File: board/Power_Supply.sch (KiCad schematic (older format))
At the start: 6 parts, among them U3 TC1015-3.3VCT713

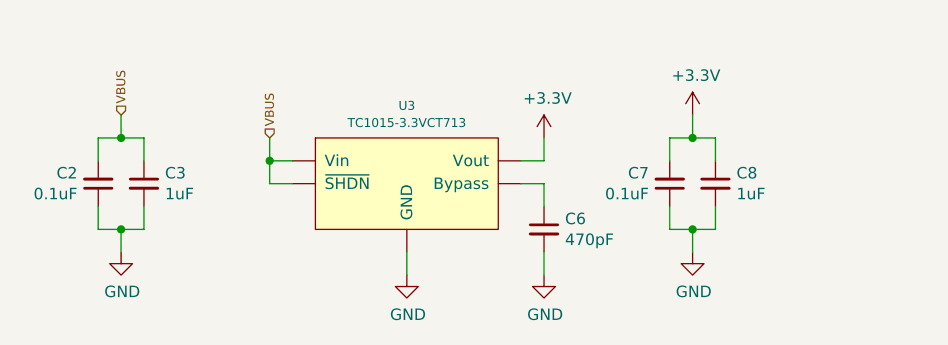
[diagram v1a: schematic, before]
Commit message: Added an LED to indicate the main board power status
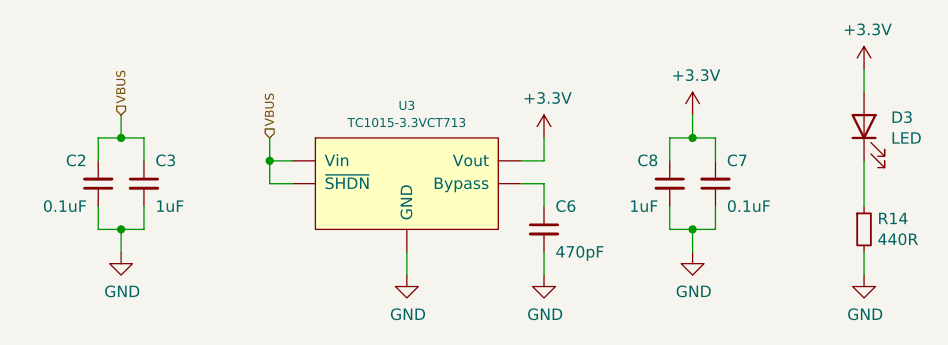
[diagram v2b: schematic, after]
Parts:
- added D3: LED, rhais_led:LED0603, symbol Device:LED
- added R14: 440R, rhais_rcl:R0603, symbol Device:R_Small
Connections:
- net +3V3: now also D3.2 (A)
- net GND: now also R14.2
- new net: D3.1 (K), R14.1
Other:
- moved on the sheet: C7, C8
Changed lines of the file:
@@
 U 1 1 5F6E72D6
 P 5600 4200
-F 0 "C6" H 5692 4246 50  0000 L CNN
-F 1 "470pF" H 5692 4155 50  0000 L CNN
+F 0 "C6" H 5650 4300 50  0000 L CNN
+F 1 "470pF" H 5650 4100 50  0000 L CNN
 F 2 "rhais_rcl:C0603" H 5600 4200 50  0001 C CNN
 F 3 "~" H 5600 4200 50  0001 C CNN
@@
 U 1 1 5F6E7C90
 P 3850 4000
-F 0 "C3" H 3942 4046 50  0000 L CNN
-F 1 "1uF" H 3942 3955 50  0000 L CNN
+F 0 "C3" H 3900 4100 50  0000 L CNN
+F 1 "1uF" H 3900 3900 50  0000 L CNN
 F 2 "rhais_rcl:C0603" H 3850 4000 50  0001 C CNN
 F 3 "~" H 3850 4000 50  0001 C CNN
@@
 U 1 1 5F6E812F
 P 3650 4000
-F 0 "C2" H 3559 3954 50  0000 R CNN
-F 1 "0.1uF" H 3559 4045 50  0000 R CNN
+F 0 "C2" H 3600 3900 50  0000 R CNN
+F 1 "0.1uF" H 3600 4100 50  0000 R CNN
 F 2 "rhais_rcl:C0603" H 3650 4000 50  0001 C CNN
 F 3 "~" H 3650 4000 50  0001 C CNN
@@
 L Device:C_Small C8
 U 1 1 5F6E94E9
+P 6150 4000
+F 0 "C8" H 6200 4100 50  0000 L CNN
+F 1 "1uF" H 6200 3900 50  0000 L CNN
+F 2 "rhais_rcl:C0603" H 6150 4000 50  0001 C CNN
+F 3 "~" H 6150 4000 50  0001 C CNN
+	1    6150 4000
+	-1   0    0    -1
+$EndComp
+$Comp
+L Device:C_Small C7
+U 1 1 5F6E94EF
 P 6350 4000
-F 0 "C8" H 6442 4046 50  0000 L CNN
-F 1 "1uF" H 6442 3955 50  0000 L CNN
+F 0 "C7" H 6300 3900 50  0000 R CNN
+F 1 "0.1uF" H 6300 4100 50  0000 R CNN
 F 2 "rhais_rcl:C0603" H 6350 4000 50  0001 C CNN
 F 3 "~" H 6350 4000 50  0001 C CNN
 	1    6350 4000
-	1    0    0    -1
-$EndComp
-$Comp
-L Device:C_Small C7
-U 1 1 5F6E94EF
-P 6150 4000
-F 0 "C7" H 6059 3954 50  0000 R CNN
-F 1 "0.1uF" H 6059 4045 50  0000 R CNN
-F 2 "rhais_rcl:C0603" H 6150 4000 50  0001 C CNN
-F 3 "~" H 6150 4000 50  0001 C CNN
-	1    6150 4000
-	1    0    0    1
+	-1   0    0    1
 $EndComp
 Text HLabel 3750 3700 1    39   Input ~ 0
@@
 	6350 3800 6350 3900
 Connection ~ 6250 3800
+$Comp
+L Device:R_Small R14
+U 1 1 5F94E976
+P 7000 4200
+F 0 "R14" H 7059 4246 50  0000 L CNN
+F 1 "440R" H 7059 4155 50  0000 L CNN
+F 2 "rhais_rcl:R0603" H 7000 4200 50  0001 C CNN
+F 3 "http://www.farnell.com/datasheets/2860681.pdf" H 7000 4200 50  0001 C CNN
+F 4 "Multicomp" H 7000 4200 50  0001 C CNN "MFR"
+F 5 "MCWR06X4700FTL" H 7000 4200 50  0001 C CNN "MPN"
+F 6 "2447374" H 7000 4200 50  0001 C CNN "OC_FARNELL"
+F 7 "https://uk.farnell.com/multicomp/mcwr06x4700ftl/res-470r-1-0-1w-0603-thick-film/dp/2447374" H 7000 4200 50  0001 C CNN "URL_FARNELL"
+	1    7000 4200
+	1    0    0    -1
+$EndComp
+$Comp
+L Device:LED D3
+U 1 1 5F94F2E8
+P 7000 3750
+F 0 "D3" V 7039 3632 50  0000 R CNN
+F 1 "LED" V 6948 3632 50  0000 R CNN
+F 2 "rhais_led:LED0603" H 7000 3750 50  0001 C CNN
+F 3 "https://www.kingbright.com/attachments/file/psearch/000/00/20160808bak/KP-1608SGC(Ver.21B).pdf" H 7000 3750 50  0001 C CNN
+F 4 "Kingbright" H 7000 3750 50  0001 C CNN "MFR"
+F 5 "8529833" H 7000 3750 50  0001 C CNN "OC_FARNELL"
+F 6 "https://uk.farnell.com/kingbright/kp-1608sgc/led-0-8mm-x-1-2mm-green-12mcd/dp/8529833" H 7000 3750 50  0001 C CNN "URL_FARNELL"
+F 7 "KP-1608SGC" H 7000 3750 50  0001 C CNN "MPN"
+	1    7000 3750
+	0    -1   -1   0
+$EndComp
+$Comp
+L power:+3.3V #PWR040
+U 1 1 5F9506D7
+P 7000 3500
+F 0 "#PWR040" H 7000 3350 50  0001 C CNN
+F 1 "+3.3V" H 7015 3673 50  0000 C CNN
+F 2 "" H 7000 3500 50  0001 C CNN
+F 3 "" H 7000 3500 50  0001 C CNN
+	1    7000 3500
+	1    0    0    -1
+$EndComp
+Wire Wire Line
+	7000 3500 7000 3600
+Wire Wire Line
+	7000 3900 7000 4100
+$Comp
+L power:GND #PWR041
+U 1 1 5F9516F3
+P 7000 4400
+F 0 "#PWR041" H 7000 4150 50  0001 C CNN
+F 1 "GND" H 7005 4227 50  0000 C CNN
+F 2 "" H 7000 4400 50  0001 C CNN
+F 3 "" H 7000 4400 50  0001 C CNN
+	1    7000 4400
+	1    0    0    -1
+$EndComp
+Wire Wire Line
+	7000 4300 7000 4400
 $EndSCHEMATC

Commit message: Fixed the state of the BOM for the PCB being horrid
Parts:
- C2, C7: MFR (none) -> Multicomp; MPN (none) -> MC0603B104J250CT; OC_FARNELL (none) -> 2310559; URL_FARNELL (none) -> https://uk.farnell.com/multicomp/mc0603b104j250ct/cap-0-1-f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
- C3, C8: MFR (none) -> Multicomp; MPN (none) -> MC0603B105K160CT; OC_FARNELL (none) -> 2320814; URL_FARNELL (none) -> https://uk.farnell.com/multicomp/mc0603b105k160ct/cap-1-f-1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
- C6: MFR (none) -> Multicomp; MPN (none) -> MC0603B471J500CT; OC_FARNELL (none) -> 2627442; URL_FARNELL (none) -> https://uk.farnell.com/multicomp/mc0603b471j500ct/cap-470pf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
- U3: MFR (none) -> Microchip; MPN (none) -> TC1015-3.3VCT713; OC_FARNELL (none) -> 1331505; URL_FARNELL (none) -> https://uk.farnell.com/microchip/tc1015-3-3vct713/ic-v-reg-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
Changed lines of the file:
@@
 F 1 "TC1015-3.3VCT713" H 5000 4266 39  0000 C CNN
 F 2 "rhais_package-smd:SOT-23-5" H 5000 4000 39  0001 C CNN
-F 3 "" H 5000 4000 39  0001 C CNN
+F 3 "http://ww1.microchip.com/downloads/en/DeviceDoc/21335e.pdf" H 5000 4000 39  0001 C CNN
+F 4 "Microchip" H 5000 4000 50  0001 C CNN "MFR"
+F 5 "1331505" H 5000 4000 50  0001 C CNN "OC_FARNELL"
+F 6 "https://uk.farnell.com/microchip/tc1015-3-3vct713/ic-v-reg-ldo-100ma-smd-sot-23/dp/1331505" H 5000 4000 50  0001 C CNN "URL_FARNELL"
+F 7 "TC1015-3.3VCT713" H 5000 4000 50  0001 C CNN "MPN"
 	1    5000 4000
 	1    0    0    -1
@@
 F 1 "470pF" H 5650 4100 50  0000 L CNN
 F 2 "rhais_rcl:C0603" H 5600 4200 50  0001 C CNN
-F 3 "~" H 5600 4200 50  0001 C CNN
+F 3 "http://www.farnell.com/datasheets/2861120.pdf" H 5600 4200 50  0001 C CNN
+F 4 "Multicomp" H 5600 4200 50  0001 C CNN "MFR"
+F 5 "MC0603B471J500CT" H 5600 4200 50  0001 C CNN "MPN"
+F 6 "2627442" H 5600 4200 50  0001 C CNN "OC_FARNELL"
+F 7 "https://uk.farnell.com/multicomp/mc0603b471j500ct/cap-470pf-50v-5-x7r-0603/dp/2627442" H 5600 4200 50  0001 C CNN "URL_FARNELL"
 	1    5600 4200
 	1    0    0    -1
@@
 F 1 "1uF" H 3900 3900 50  0000 L CNN
 F 2 "rhais_rcl:C0603" H 3850 4000 50  0001 C CNN
-F 3 "~" H 3850 4000 50  0001 C CNN
+F 3 "http://www.farnell.com/datasheets/2860632.pdf" H 3850 4000 50  0001 C CNN
+F 4 "Multicomp" H 3850 4000 50  0001 C CNN "MFR"
+F 5 "MC0603B105K160CT" H 3850 4000 50  0001 C CNN "MPN"
+F 6 "2320814" H 3850 4000 50  0001 C CNN "OC_FARNELL"
+F 7 "https://uk.farnell.com/multicomp/mc0603b105k160ct/cap-1-f-16v-10-x7r-0603/dp/2320814" H 3850 4000 50  0001 C CNN "URL_FARNELL"
 	1    3850 4000
 	1    0    0    -1
@@
 F 1 "0.1uF" H 3600 4100 50  0000 R CNN
 F 2 "rhais_rcl:C0603" H 3650 4000 50  0001 C CNN
-F 3 "~" H 3650 4000 50  0001 C CNN
+F 3 "http://www.farnell.com/datasheets/1870456.pdf" H 3650 4000 50  0001 C CNN
+F 4 "Multicomp" H 3650 4000 50  0001 C CNN "MFR"
+F 5 "MC0603B104J250CT" H 3650 4000 50  0001 C CNN "MPN"
+F 6 "2310559" H 3650 4000 50  0001 C CNN "OC_FARNELL"
+F 7 "https://uk.farnell.com/multicomp/mc0603b104j250ct/cap-0-1-f-25v-5-x7r-0603-reel/dp/2310559" H 3650 4000 50  0001 C CNN "URL_FARNELL"
 	1    3650 4000
 	1    0    0    1
@@
 F 1 "1uF" H 6200 3900 50  0000 L CNN
 F 2 "rhais_rcl:C0603" H 6150 4000 50  0001 C CNN
-F 3 "~" H 6150 4000 50  0001 C CNN
+F 3 "http://www.farnell.com/datasheets/2860632.pdf" H 6150 4000 50  0001 C CNN
+F 4 "Multicomp" H 6150 4000 50  0001 C CNN "MFR"
+F 5 "MC0603B105K160CT" H 6150 4000 50  0001 C CNN "MPN"
+F 6 "2320814" H 6150 4000 50  0001 C CNN "OC_FARNELL"
+F 7 "https://uk.farnell.com/multicomp/mc0603b105k160ct/cap-1-f-16v-10-x7r-0603/dp/2320814" H 6150 4000 50  0001 C CNN "URL_FARNELL"
 	1    6150 4000
 	-1   0    0    -1
@@
 F 1 "0.1uF" H 6300 4100 50  0000 R CNN
 F 2 "rhais_rcl:C0603" H 6350 4000 50  0001 C CNN
-F 3 "~" H 6350 4000 50  0001 C CNN
+F 3 "http://www.farnell.com/datasheets/1870456.pdf" H 6350 4000 50  0001 C CNN
+F 4 "Multicomp" H 6350 4000 50  0001 C CNN "MFR"
+F 5 "MC0603B104J250CT" H 6350 4000 50  0001 C CNN "MPN"
+F 6 "2310559" H 6350 4000 50  0001 C CNN "OC_FARNELL"
+F 7 "https://uk.farnell.com/multicomp/mc0603b104j250ct/cap-0-1-f-25v-5-x7r-0603-reel/dp/2310559" H 6350 4000 50  0001 C CNN "URL_FARNELL"
 	1    6350 4000
 	-1   0    0    1
